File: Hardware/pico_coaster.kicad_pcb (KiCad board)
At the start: 2 copper layers, 90 x 90 mm, 142 parts, among them J3 Conn_02x06_Odd_Even, J4 Conn_01x04, J5 USB_C_Receptacle_USB2.0, SW1 SW_Push, SW2 SW_Push, SW3 SW_Push, SW4 SW_Push, SW5 SW_Push, SW6 SW_Push, U1 NCP1117-3.3_SOT223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

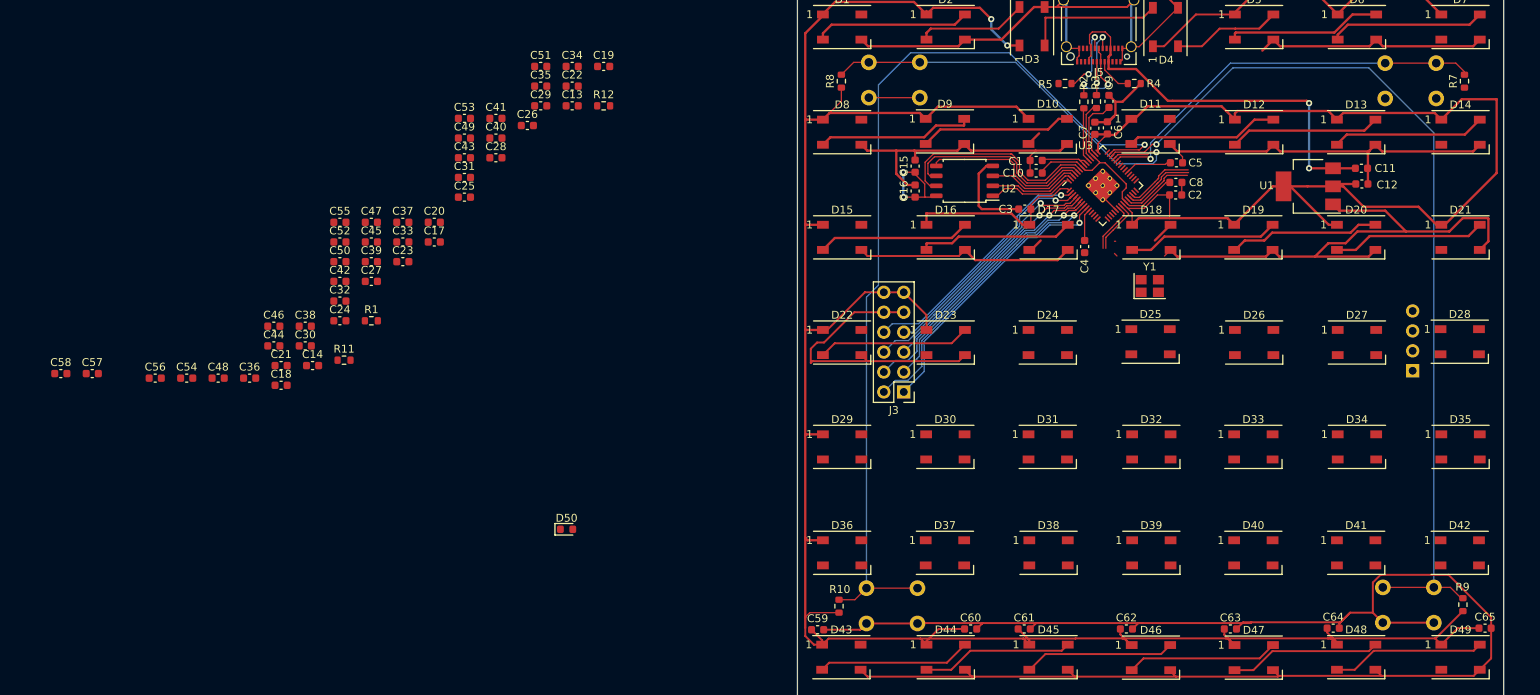
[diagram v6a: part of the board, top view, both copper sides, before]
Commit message: Routing Bottom row 3 RGB LEDs completed
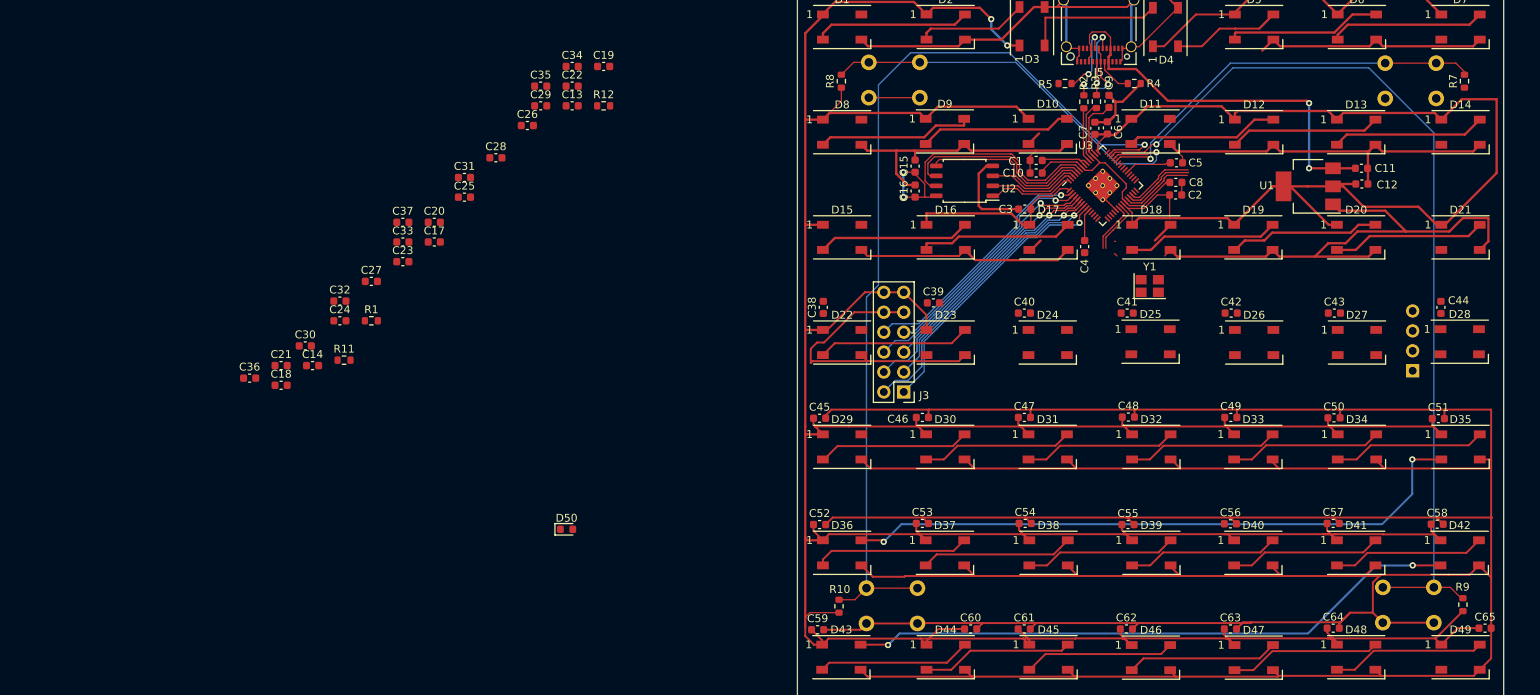
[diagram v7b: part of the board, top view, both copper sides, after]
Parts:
- moved C58 176.4 mm to (246.5, 103.2)
- moved C57 159.3 mm to (233.3, 103.0)
- moved C44 148.8 mm to (247.0, 75.5), turned to 90 degrees
- moved C56 138.3 mm to (220.2, 103.1)
- moved C50 128.2 mm to (233.4, 89.6)
- moved C51 122.9 mm to (246.7, 89.7)
- moved C48 116.1 mm to (207.2, 89.5)
- moved C42 113.6 mm to (220.3, 76.2)
- moved C43 112.6 mm to (233.4, 76.2)
- moved C54 108.4 mm to (194.0, 103.0)
- moved C55 107.6 mm to (207.1, 103.2)
- moved C49 103.9 mm to (220.2, 89.5)
- moved C47 86.9 mm to (193.9, 89.5)
- moved C41 84.2 mm to (207.0, 76.2)
- moved C46 83.5 mm to (180.9, 89.5)
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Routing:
- net GND: track 559.2 -> 935.2 mm
- net +3V3: track 544.6 -> 746.0 mm
- net Net-(D35-Pad2): track 0.00 -> 80.9 mm, vias 0 -> 2
- net Net-(D42-Pad2): track 0.00 -> 78.1 mm, vias 0 -> 2
- net Net-(D36-Pad2): track 0.00 -> 19.8 mm
- net Net-(D31-Pad2): track 0.00 -> 19.4 mm
- net Net-(D41-Pad2): track 0.00 -> 19.4 mm
- net Net-(D37-Pad2): track 0.00 -> 19.4 mm
- net Net-(D34-Pad2): track 0.00 -> 19.4 mm
- net Net-(D33-Pad2): track 0.00 -> 19.4 mm
- net Net-(D29-Pad2): track 0.00 -> 19.4 mm
- net Net-(D40-Pad2): track 0.00 -> 19.3 mm
- net Net-(D38-Pad2): track 0.00 -> 19.3 mm
- net Net-(D30-Pad2): track 0.00 -> 19.3 mm
- net Net-(D39-Pad2): track 0.00 -> 19.2 mm
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
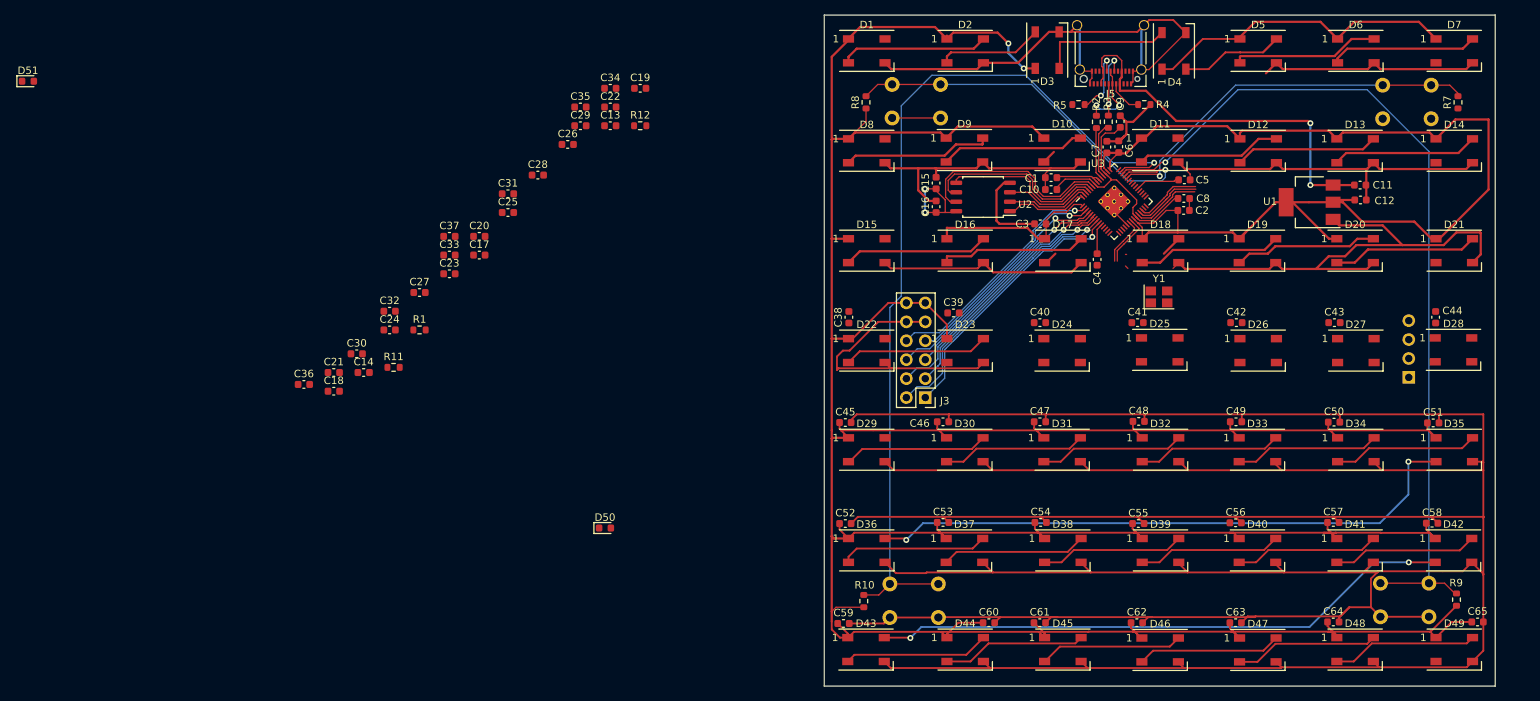
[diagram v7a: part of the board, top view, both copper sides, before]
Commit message: Finish layout for the top three LED rows
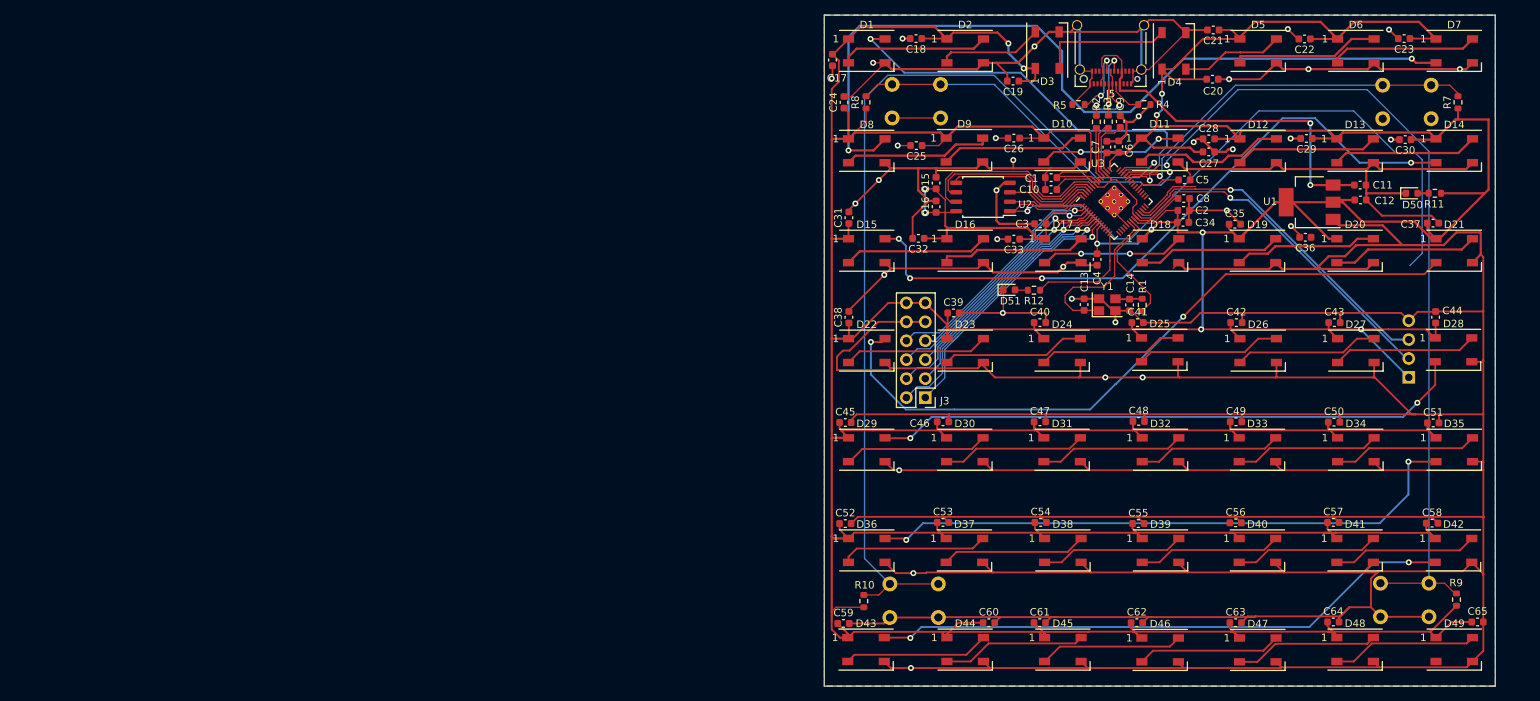
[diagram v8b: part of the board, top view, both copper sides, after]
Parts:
- moved C30 143.5 mm to (242.9, 51.7), turned to 180 degrees
- moved R11 141.6 mm to (246.9, 58.9), turned to 180 degrees
- moved C36 135.8 mm to (229.5, 64.8), turned to 180 degrees
- moved D51 134.6 mm to (189.8, 71.8)
- moved C37 131.9 mm to (246.7, 62.9)
- moved C23 131.9 mm to (242.8, 38.1), turned to 180 degrees
- moved C21 126.6 mm to (217.2, 37.0), turned to 180 degrees
- moved D50 117.2 mm to (243.8, 58.9)
- moved C27 107.5 mm to (216.6, 53.4)
- moved C14 103.1 mm to (205.9, 73.9), turned to 270 degrees
- moved C20 100.6 mm to (217.1, 43.6)
- moved C29 97.4 mm to (229.7, 51.5), turned to 180 degrees
- moved R1 97.0 mm to (207.7, 73.9), turned to 90 degrees
- moved C22 93.6 mm to (229.4, 38.2), turned to 180 degrees
- moved C18 91.3 mm to (177.3, 38.1), turned to 180 degrees
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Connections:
- R12 pad 1: GPIO_24 -> GPIO_11
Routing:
- net GND: track 935.2 -> 1208.9 mm, vias 0 -> 33
- net +3V3: track 746.0 -> 967.3 mm, vias 4 -> 11
- net Net-(D7-Pad2): track 0.00 -> 111.2 mm, vias 0 -> 2
- net Net-(D21-Pad2): track 0.00 -> 92.3 mm, vias 0 -> 2
- net Net-(D14-Pad2): track 0.00 -> 89.7 mm, vias 0 -> 4
- net QSPI_SS: track 11.1 -> 93.2 mm, vias 0 -> 1
- net Net-(D28-Pad2): track 0.00 -> 79.9 mm, vias 0 -> 2
- net GPIO_25: track 0.00 -> 57.4 mm, vias 0 -> 2
- net SWCLK: track 9.49 -> 47.4 mm, vias 0 -> 1
- net SWDIO: track 9.32 -> 46.3 mm, vias 0 -> 1
- net Net-(D25-Pad2): track 0.00 -> 19.4 mm
- net Net-(D27-Pad2): track 0.00 -> 19.4 mm
- net Net-(D24-Pad2): track 0.00 -> 19.4 mm
- net Net-(D26-Pad2): track 0.00 -> 19.3 mm
- net Net-(D23-Pad2): track 0.00 -> 19.2 mm
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- added copper zone on B.Cu, net GND
